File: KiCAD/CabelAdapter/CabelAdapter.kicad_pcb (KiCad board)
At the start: 4 copper layers, 100 x 90 mm, 24 parts, among them J1 8P8C, J10 Conn_02x08_Odd_Even, J11 Conn_Coaxial, J12 Conn_01x04_Pin, J13 Conn_01x08_Pin, J14 Conn_Coaxial, J15 Screw_Terminal_01x08, J16 Conn_Coaxial, J17 Conn_01x04_Pin, J18 Conn_Coaxial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

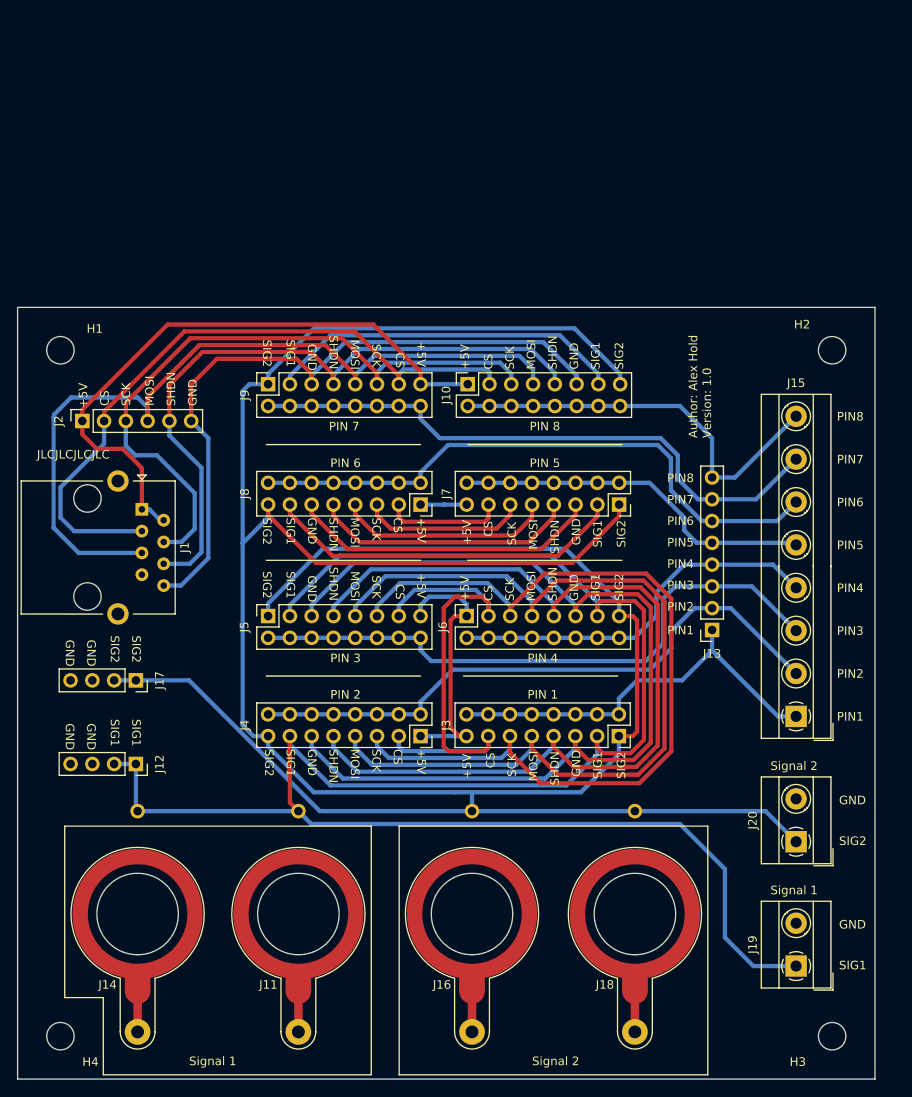
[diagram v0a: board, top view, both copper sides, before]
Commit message: Added images for newly produced PCBs + added 3D models
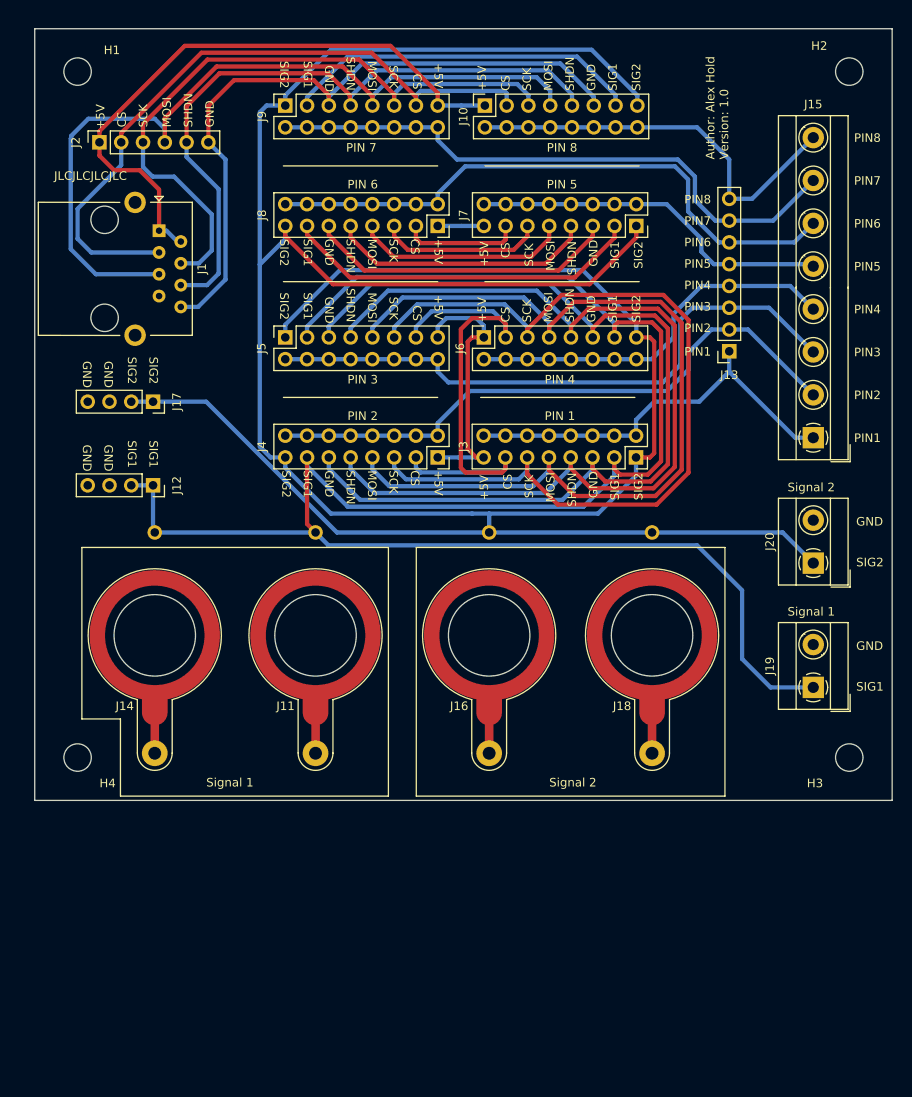
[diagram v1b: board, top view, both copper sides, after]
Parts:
- moved H1 32.6 mm to (87.0, 52.5)
- moved H2 32.6 mm to (177.0, 52.5)
- moved H3 32.6 mm to (177.0, 132.5)
- moved H4 32.6 mm to (87.0, 132.5)
- moved J1 32.6 mm to (96.5, 71.1)
- moved J11 32.6 mm to (114.8, 118.2)
- moved J12 32.6 mm to (95.8, 100.8)
- moved J13 32.6 mm to (163.0, 85.1)
- moved J14 32.6 mm to (96.0, 118.2)
- moved J15 32.6 mm to (172.8, 77.7)
- moved J16 32.6 mm to (135.0, 118.2)
- moved J17 32.6 mm to (95.8, 91.0)
- moved J18 32.6 mm to (154.0, 118.2)
- moved J19 32.6 mm to (172.8, 124.3)
- moved J2 32.6 mm to (89.5, 60.8)
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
